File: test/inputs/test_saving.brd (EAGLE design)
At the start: 160 x 100 mm, 17 parts

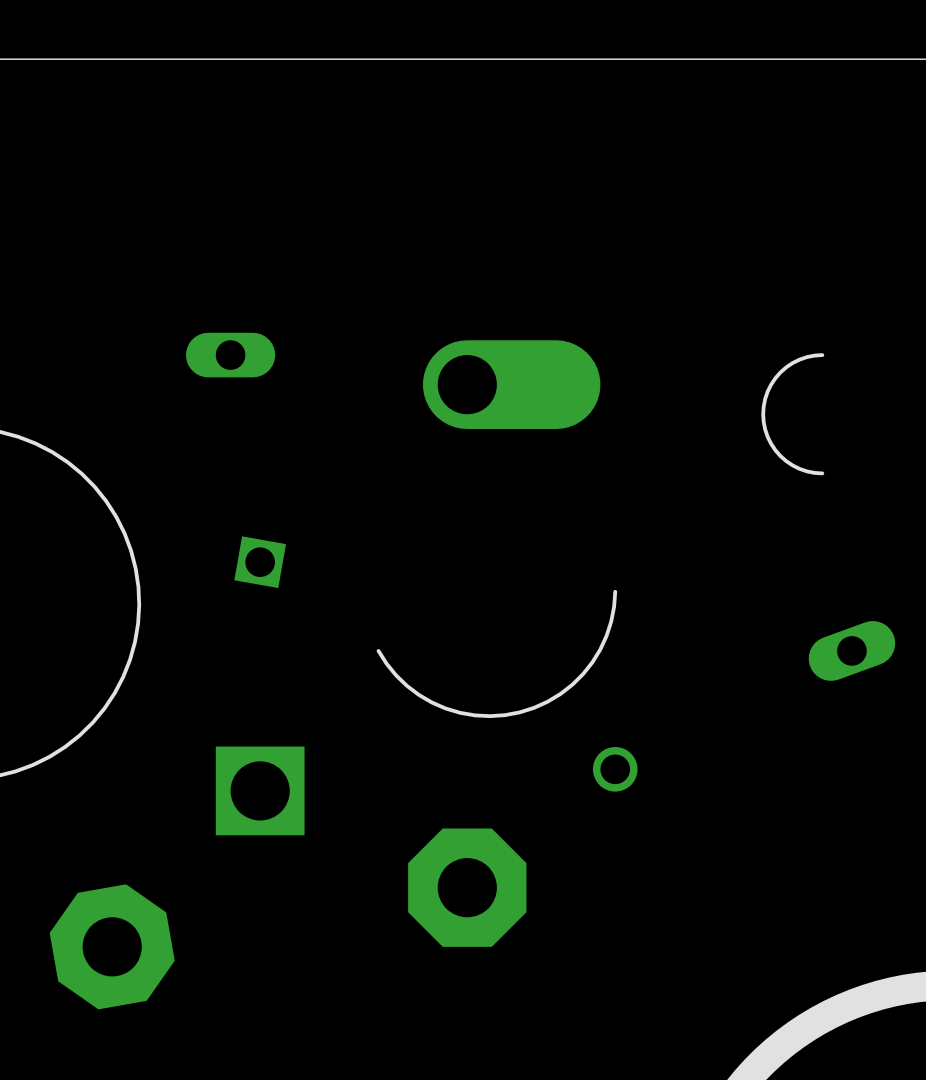
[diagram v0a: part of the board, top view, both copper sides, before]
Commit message: Improvements for ShapelySwoop to use DRU
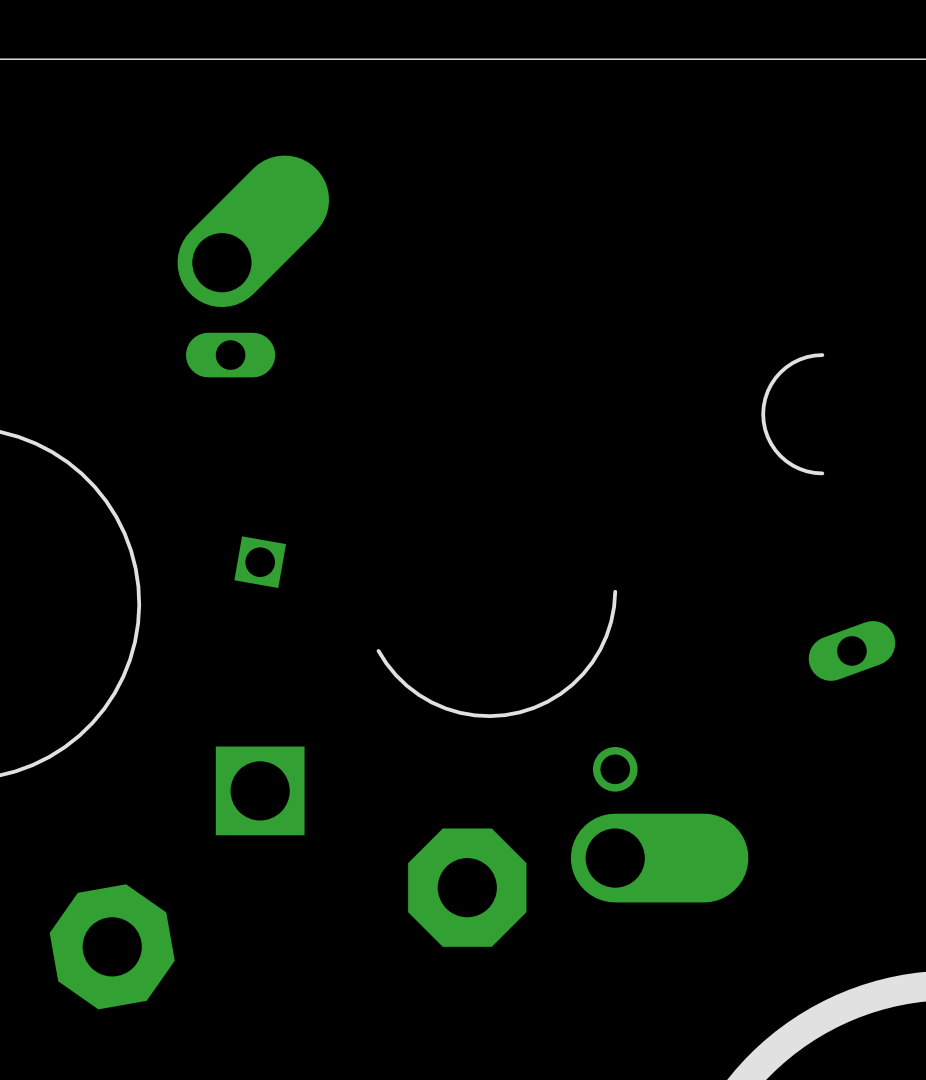
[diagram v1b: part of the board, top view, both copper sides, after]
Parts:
- added TEST-PAD3: TEST-PAD1, Swoop-Test-Packages:TEST-PAD1
- moved TEST-PAD1 16.8 mm to (129.0, 72.0)
